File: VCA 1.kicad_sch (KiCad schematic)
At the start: 87 parts, among them J1 Eurorack 2x8hs, J10 CV2, J11 IN2, J12 IN 1x8h, J13 OUT1, J14 OUT2, J15 IN 1x8s, J2 OUT 1x3s, J3 CV 1x9s, J5 CV 1x9h, J6 OUT 1x3h, J8 CV1, J9 IN1, Q1 2N3904, Q2 2N3904, U1 TL074, U2 AS2164

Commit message: Updated schematic and image
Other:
- moved on the sheet: C12, J10, R13, R14, R15, R16, R24, RV10, RV2, RV4, RV9, U1B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

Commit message: Noted linearization components
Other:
- note added: "Linearization 1 A"
- note added: "Linearization 1 B"
- note added: "Linearization 2 A"
- note added: "Linearization 2 B"
- note removed: "VCA 2 Input"
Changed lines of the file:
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@@
 	)
 	(rectangle
-		(start 17.145 117.475)
-		(end 251.46 236.22)
+		(start 15.24 205.105)
+		(end 80.01 234.315)
 		(stroke
 			(width 0)
@@
 	)
 	(rectangle
-		(start 17.145 13.97)
-		(end 251.46 117.475)
+		(start 17.145 43.18)
+		(end 81.915 72.39)
 		(stroke
 			(width 0)
@@
 	(text "Curve 2"
 		(exclude_from_sim no)
-		(at 140.462 142.494 0)
+		(at 135.382 156.972 0)
 		(effects
 			(font
@@
 		)
 	)
+	(text "Linearization 2 A"
+		(exclude_from_sim no)
+		(at 24.638 232.41 0)
+		(effects
+			(font
+				(size 1.27 1.27)
+			)
+		)
+	)
 	(text "Offset 2"
 		(exclude_from_sim no)
@@
 	(text "Curve 1"
 		(exclude_from_sim no)
-		(at 141.224 104.394 0)
+		(at 134.366 118.618 0)
+		(effects
+			(font
+				(size 1.27 1.27)
+			)
+		)
+	)
+	(text "Linearization 1 B"
+		(exclude_from_sim no)
+		(at 138.938 104.648 0)
 		(effects
 			(font
@@
 	(text "VCA 2 Output"
 		(exclude_from_sim no)
-		(at 299.466 144.018 0)
+		(at 260.096 98.298 0)
 		(effects
 			(font
@@
 	(text "VCA 1 Output"
 		(exclude_from_sim no)
-		(at 298.958 32.512 0)
+		(at 260.096 91.694 0)
 		(effects
 			(font
@@
 		)
 	)
+	(text "Linearization 2 B"
+		(exclude_from_sim no)
+		(at 139.7 143.002 0)
+		(effects
+			(font
+				(size 1.27 1.27)
+			)
+		)
+	)
 	(text "Hagiwo"
 		(exclude_from_sim yes)
@@
 		)
 	)
-	(text "VCA 1 Input"
+	(text "Linearization 1 A"
 		(exclude_from_sim no)
-		(at 25.4 17.78 0)
+		(at 26.924 71.12 0)
 		(effects
 			(font
@@
 		)
 	)
-	(text "Dual VCA I (main and control boards)"
+	(text "VCA 1 Input"
 		(exclude_from_sim no)
-		(at 347.726 276.606 0)
+		(at 136.398 53.086 0)
 		(effects
 			(font
-				(size 2.54 2.54)
+				(size 1.27 1.27)
 			)
 		)
 	)
-	(text "Offset 1"
+	(text "Dual VCA I (main and control boards)"
 		(exclude_from_sim no)
-		(at 23.622 102.87 0)
+		(at 347.726 276.606 0)
 		(effects
 			(font
-				(size 1.27 1.27)
+				(size 2.54 2.54)
 			)
 		)
 	)
-	(text "VCA 2 Input"
+	(text "Offset 1"
 		(exclude_from_sim no)
-		(at 25.146 233.426 0)
+		(at 23.622 102.87 0)
 		(effects
 			(font
@@
 	)
 	(junction
+		(at 73.66 195.58)
+		(diameter 0)
+		(color 0 0 0 0)
+	)
+	(junction
 		(at 140.97 243.84)
 		(diameter 0)
@@
 	)
 	(junction
-		(at 78.74 195.58)
-		(diameter 0)
-		(color 0 0 0 0)
-	)
-	(junction
 		(at 201.93 274.32)
 		(diameter 0)
@@
 		)
 	)
+	(polyline
+		(pts
+			(xy 130.81 140.335) (xy 130.81 160.02)
+		)
+		(stroke
+			(width 0)
+			(type default)
+		)
+	)
 	(wire
 		(pts
@@
 		)
 	)
+	(polyline
+		(pts
+			(xy 203.835 119.38) (xy 156.845 119.38)
+		)
+		(stroke
+			(width 0)
+			(type default)
+		)
+	)
 	(wire
 		(pts
@@
 	(wire
 		(pts
-			(xy 78.74 195.58) (xy 146.05 195.58)
-		)
-		(stroke
-			(width 0)
-			(type default)
-		)
-	)
-	(wire
-		(pts
 			(xy 24.13 187.96) (xy 24.13 191.77)
 		)
@@
 		)
 	)
+	(polyline
+		(pts
+			(xy 152.4 120.65) (xy 152.4 116.84)
+		)
+		(stroke
+			(width 0)
+			(type default)
+		)
+	)
 	(wire
 		(pts
@@
 		)
 	)
+	(polyline
+		(pts
+			(xy 129.54 102.87) (xy 151.13 102.87)
+		)
+		(stroke
+			(width 0)
+			(type default)
+		)
+	)
 	(wire
 		(pts
@@
 		)
 	)
+	(polyline
+		(pts
+			(xy 129.54 120.65) (xy 152.4 120.65)
+		)
+		(stroke
+			(width 0)
+			(type default)
+		)
+	)
 	(wire
 		(pts
@@
 		)
 	)
+	(polyline
+		(pts
+			(xy 250.19 98.425) (xy 223.52 98.425)
+		)
+		(stroke
+			(width 0)
+			(type default)
+		)
+	)
 	(wire
 		(pts
@@
 	(wire
 		(pts
-			(xy 78.74 218.44) (xy 69.85 218.44)
+			(xy 73.66 218.44) (xy 69.85 218.44)
 		)
 		(stroke
@@
 		)
 	)
+	(polyline
+		(pts
+			(xy 152.4 116.84) (xy 250.19 116.84)
+		)
+		(stroke
+			(width 0)
+			(type default)
+		)
+	)
 	(wire
 		(pts
@@
 	(wire
 		(pts
-			(xy 78.74 195.58) (xy 78.74 218.44)
+			(xy 73.66 195.58) (xy 73.66 218.44)
 		)
 		(stroke
@@
 		)
 	)
+	(polyline
+		(pts
+			(xy 156.845 119.38) (xy 156.845 140.335)
+		)
+		(stroke
+			(width 0)
+			(type default)
+		)
+	)
 	(wire
 		(pts
@@
 		)
 	)
+	(polyline
+		(pts
+			(xy 223.52 109.22) (xy 151.13 109.22)
+		)
+		(stroke
+			(width 0)
+			(type default)
+		)
+	)
 	(wire
 		(pts
@@
 	(wire
 		(pts
+			(xy 73.66 195.58) (xy 146.05 195.58)
+		)
+		(stroke
+			(width 0)
+			(type default)
+		)
+	)
+	(wire
+		(pts
 			(xy 140.97 243.84) (xy 127 243.84)
 		)
@@
 		)
 	)
+	(polyline
+		(pts
+			(xy 130.81 160.02) (xy 203.835 160.02)
+		)
+		(stroke
+			(width 0)
+			(type default)
+		)
+	)
 	(wire
 		(pts
@@
 		)
 	)
+	(polyline
+		(pts
+			(xy 151.13 109.22) (xy 151.13 102.87)
+		)
+		(stroke
+			(width 0)
+			(type default)
+		)
+	)
 	(wire
 		(pts
@@
 	(wire
 		(pts
-			(xy 41.91 195.58) (xy 78.74 195.58)
+			(xy 41.91 195.58) (xy 73.66 195.58)
+		)
+		(stroke
+			(width 0)
+			(type default)
+		)
+	)
+	(polyline
+		(pts
+			(xy 250.19 116.84) (xy 250.19 98.425)
 		)
 		(stroke
@@
 		)
 	)
+	(polyline
+		(pts
+			(xy 203.835 160.02) (xy 203.835 119.38)
+		)
+		(stroke
+			(width 0)
+			(type default)
+		)
+	)
 	(wire
 		(pts
@@
 		)
 	)
+	(polyline
+		(pts
+			(xy 156.845 140.335) (xy 130.81 140.335)
+		)
+		(stroke
+			(width 0)
+			(type default)
+		)
+	)
 	(wire
 		(pts
@@
 		)
 	)
+	(polyline
+		(pts
+			(xy 223.52 98.425) (xy 223.52 109.22)
+		)
+		(stroke
+			(width 0)
+			(type default)
+		)
+	)
 	(wire
 		(pts
@@
 		)
 	)
+	(polyline
+		(pts
+			(xy 129.54 102.87) (xy 129.54 120.65)
+		)
+		(stroke
+			(width 0)
+			(type default)
+		)
+	)
 	(global_label "+12v"
 		(shape input)
@@
 		)
 	)
+	(group ""
+		(members "18a44e6c-de5b-467a-8f2e-db9e40b2f192" "26d99882-d493-48b8-8b53-ef1b25249a56"
+			"335e110c-c7a5-42e0-965f-61530e30d26d" "35f6677c-5b62-4938-b17b-062d7b1850b7"
+			"7b091e6f-4273-460f-bf15-8d6bc277b69b" "a904838e-bbb1-44ab-9fbb-02d583ba5790"
+			"b56eea77-ddf2-493a-affa-bebb6470614a" "d29784d0-988b-4366-947c-30e8e71c4bf2"
+			"f483f174-9161-47e0-90b6-0b6b0535353c" "ff328fe6-7960-4840-bb69-712337915f44"
+		)
+	)
+	(group ""
+		(members "01b665f1-7e63-4283-a37a-9746674eea88" "06bd41dc-a293-40ec-972a-06a894a96dc2"
+			"9f5f978c-7975-466a-84ba-87b8600012bb" "b4068527-1d47-46ce-bbba-b00ad5667bf6"
+			"ea6af55a-41a7-4d35-8ed7-e8c048290715" "f143c6ff-58e2-4165-997b-5711abf60db6"
+		)
+	)

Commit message: New simulation, updated design after breadboard test.
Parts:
- added R19, R20: 390R, Resistor_THT:R_Axial_DIN0204_L3.6mm_D1.6mm_P2.54mm_Vertical, symbol Device:R
- R24, R8: value 2K2 -> 3K3
- RV5, RV6: value 10K B -> 1K B
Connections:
- net at U2.6 (CV): now also R19.1; no longer J15.3 (Pin_3)
- net at J15.7 (Pin_7): now also R20.2; no longer U2.14 (CV)
- new net: J15.3 (Pin_3), R19.2
- new net: R20.1, U2.14 (CV)
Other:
- note added: "Curve selection 1"
- note added: "Curve selection 2"
- note added: "Input stage 1"
- note added: "Input stage 2"
- note added: "Linearization 1"
- note added: "Linearization 2"
- note added: "Output 1"
- note added: "Output 2"
- note removed: "Linearization 1 A"
- note removed: "Linearization 1 B"
- note removed: "Linearization 2 A"
- note removed: "Linearization 2 B"
- note removed: "VCA 1 Output"
- note removed: "VCA 2 Output"
- moved on the sheet: J10, RV2, RV4

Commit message: Updated curve values to match breadboard
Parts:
- added C15, C16: 10uF t, Capacitor_THT:CP_Radial_Tantal_D4.5mm_P2.50mm, symbol Device:C_Polarized
- R24, R8: value 3K3 -> 2K2
- RV5, RV6: value 1K B -> 10K B
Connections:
- net at R10.1, U2.2 (IN): now also C15.2; no longer R9.2
- net at R18.1, U2.10 (IN): now also C16.2; no longer R17.2
- new net: C16.1, R17.2
- new net: C15.1, R9.2
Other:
- moved on the sheet: C10, C13, R10, R18, R9

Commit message: Removed uneeded resistor
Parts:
- removed R19, R20: 390R, Resistor_THT:R_Axial_DIN0204_L3.6mm_D1.6mm_P2.54mm_Vertical, symbol Device:R
- R18: footprint Resistor_THT:R_Axial_DIN0204_L3.6mm_D1.6mm_P7.62mm_Horizontal -> Resistor_THT:R_Axial_DIN0204_L3.6mm_D1.6mm_P2.54mm_Vertical
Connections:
- net at U2.6 (CV): now also J15.3 (Pin_3)
- net at J15.7 (Pin_7): now also U2.14 (CV)
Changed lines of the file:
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@@
 	(wire
 		(pts
-			(xy 205.74 144.78) (xy 205.74 227.33)
+			(xy 205.74 123.19) (xy 205.74 227.33)
 		)
 		(stroke
@@
 	(wire
 		(pts
-			(xy 209.55 113.03) (xy 210.82 113.03)
-		)
-		(stroke
-			(width 0)
-			(type default)
-		)
-	)
-	(wire
-		(pts
 			(xy 321.31 52.07) (xy 314.96 52.07)
 		)
@@
 	(wire
 		(pts
-			(xy 199.39 113.03) (xy 201.93 113.03)
+			(xy 199.39 113.03) (xy 210.82 113.03)
 		)
 		(stroke
@@
 		)
 	)
-	(wire
-		(pts
-			(xy 205.74 123.19) (xy 205.74 137.16)
-		)
-		(stroke
-			(width 0)
-			(type default)
-		)
-	)
 	(polyline
 		(pts
@@
 			)
 		)
-		(property "Footprint" "Resistor_THT:R_Axial_DIN0204_L3.6mm_D1.6mm_P7.62mm_Horizontal"
+		(property "Footprint" "Resistor_THT:R_Axial_DIN0204_L3.6mm_D1.6mm_P2.54mm_Vertical"
 			(at 247.142 133.35 90)
 			(hide yes)
@@
 	)
 	(symbol
-		(lib_id "Device:R")
-		(at 205.74 113.03 270)
-		(unit 1)
-		(body_style 1)
-		(exclude_from_sim no)
-		(in_bom yes)
-		(on_board yes)
-		(in_pos_files yes)
-		(dnp no)
-		(fields_autoplaced yes)
-		(property "Reference" "R19"
-			(at 205.74 106.68 90)
-			(show_name no)
-			(do_not_autoplace no)
-			(effects
-				(font
-					(size 1.27 1.27)
-				)
-			)
-		)
-		(property "Value" "390R"
-			(at 205.74 109.22 90)
-			(show_name no)
-			(do_not_autoplace no)
-			(effects
-				(font
-					(size 1.27 1.27)
-				)
-			)
-		)
-		(property "Footprint" "Resistor_THT:R_Axial_DIN0204_L3.6mm_D1.6mm_P2.54mm_Vertical"
-			(at 205.74 111.252 90)
-			(hide yes)
-			(show_name no)
-			(do_not_autoplace no)
-			(effects
-				(font
-					(size 1.27 1.27)
-				)
-			)
-		)
-		(property "Datasheet" ""
-			(at 205.74 113.03 0)
-			(hide yes)
-			(show_name no)
-			(do_not_autoplace no)
-			(effects
-				(font
-					(size 1.27 1.27)
-				)
-			)
-		)
-		(property "Description" "Resistor"
-			(at 205.74 113.03 0)
-			(hide yes)
-			(show_name no)
-			(do_not_autoplace no)
-			(effects
-				(font
-					(size 1.27 1.27)
-				)
-			)
-		)
-		(pin "2"
-		)
-		(pin "1"
-		)
-		(instances
-			(project "VCA 1"
-				(path "/eb1652b6-57da-4a0e-88a4-449907a19840"
-					(reference "R19")
-					(unit 1)
-				)
-			)
-		)
-	)
-	(symbol
 		(lib_id "Connector_Audio:AudioJack2_SwitchT")
 		(at 25.4 140.97 0)
@@
 					(unit 1)
 				)
-			)
-		)
-	)
-	(symbol
-		(lib_id "Device:R")
-		(at 205.74 140.97 180)
-		(unit 1)
-		(body_style 1)
-		(exclude_from_sim no)
-		(in_bom yes)
-		(on_board yes)
-		(in_pos_files yes)
-		(dnp no)
-		(fields_autoplaced yes)
-		(property "Reference" "R20"
-			(at 208.28 139.6999 0)
-			(show_name no)
-			(do_not_autoplace no)
-			(effects
-				(font
-					(size 1.27 1.27)
-				)
-				(justify right)
-			)
-		)
-		(property "Value" "390R"
-			(at 208.28 142.2399 0)
-			(show_name no)
-			(do_not_autoplace no)
-			(effects
-				(font
-					(size 1.27 1.27)
-				)
-				(justify right)
-			)
-		)
-		(property "Footprint" "Resistor_THT:R_Axial_DIN0204_L3.6mm_D1.6mm_P2.54mm_Vertical"
-			(at 207.518 140.97 90)
-			(hide yes)
-			(show_name no)
-			(do_not_autoplace no)
-			(effects
-				(font
-					(size 1.27 1.27)
-				)
-			)
-		)
-		(property "Datasheet" ""
-			(at 205.74 140.97 0)
-			(hide yes)
-			(show_name no)
-			(do_not_autoplace no)
-			(effects
-				(font
-					(size 1.27 1.27)
-				)
-			)
-		)
-		(property "Description" "Resistor"
-			(at 205.74 140.97 0)
-			(hide yes)
-			(show_name no)
-			(do_not_autoplace no)
-			(effects
-				(font
-					(size 1.27 1.27)
-				)
-			)
-		)
-		(pin "2"
-		)
-		(pin "1"
-		)
-		(instances
-			(project "VCA 1"
-				(path "/eb1652b6-57da-4a0e-88a4-449907a19840"
-					(reference "R20")
-					(unit 1)
-				)

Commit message: Reworked R values for 0-8V CV
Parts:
- R15, R6: value 33K -> 10K
- R24, R8: value 2K2 -> 15K
- RV8: value 10K -> 20K
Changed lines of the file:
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@@
 	(text "Offset 2"
 		(exclude_from_sim no)
-		(at 24.13 140.97 0)
+		(at 20.828 122.174 0)
 		(effects
 			(font
@@
 		(fields_autoplaced yes)
 		(property "Reference" "R6"
-			(at 40.64 36.83 90)
+			(at 40.64 26.67 90)
 			(show_name no)
 			(do_not_autoplace no)
@@
 			)
 		)
-		(property "Value" "33K"
-			(at 40.64 39.37 90)
+		(property "Value" "10K"
+			(at 40.64 29.21 90)
 			(show_name no)
 			(do_not_autoplace no)
@@
 		(fields_autoplaced yes)
 		(property "Reference" "R15"
-			(at 38.1 199.39 90)
+			(at 38.1 189.23 90)
 			(show_name no)
 			(do_not_autoplace no)
@@
 			)
 		)
-		(property "Value" "33K"
-			(at 38.1 201.93 90)
+		(property "Value" "10K"
+			(at 38.1 191.77 90)
 			(show_name no)
 			(do_not_autoplace no)
@@
 			)
 		)
-		(property "Value" "10K"
+		(property "Value" "20K"
 			(at 24.13 57.1499 0)
 			(show_name no)
@@
 			)
 		)
-		(property "Value" "2K2"
+		(property "Value" "15K"
 			(at 203.2 142.2399 0)
 			(show_name no)
@@
 			)
 		)
-		(property "Value" "2K2"
+		(property "Value" "15K"
 			(at 240.03 99.06 90)
 			(show_name no)

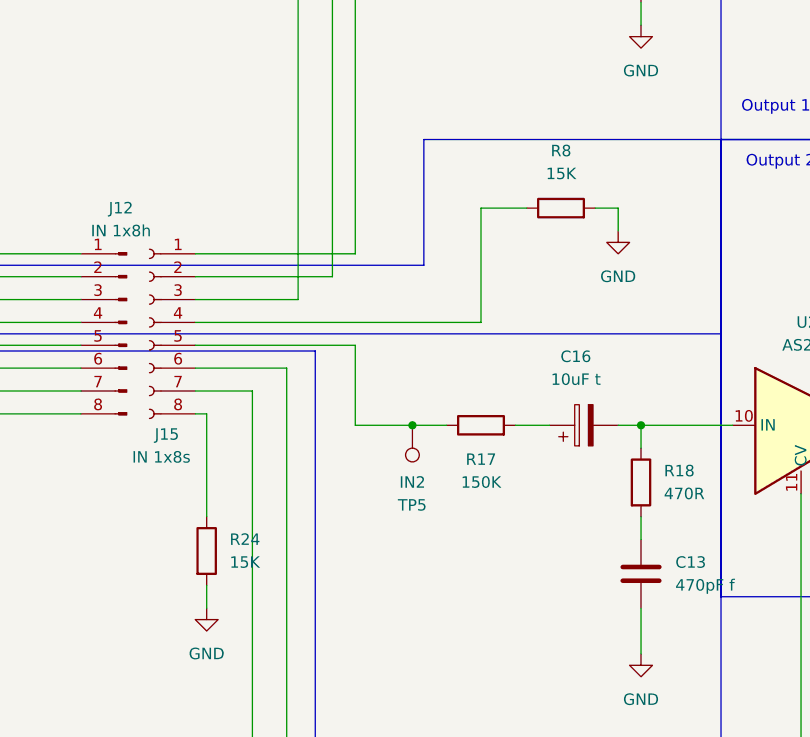
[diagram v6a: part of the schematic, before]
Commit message: Updated Curve to GND R
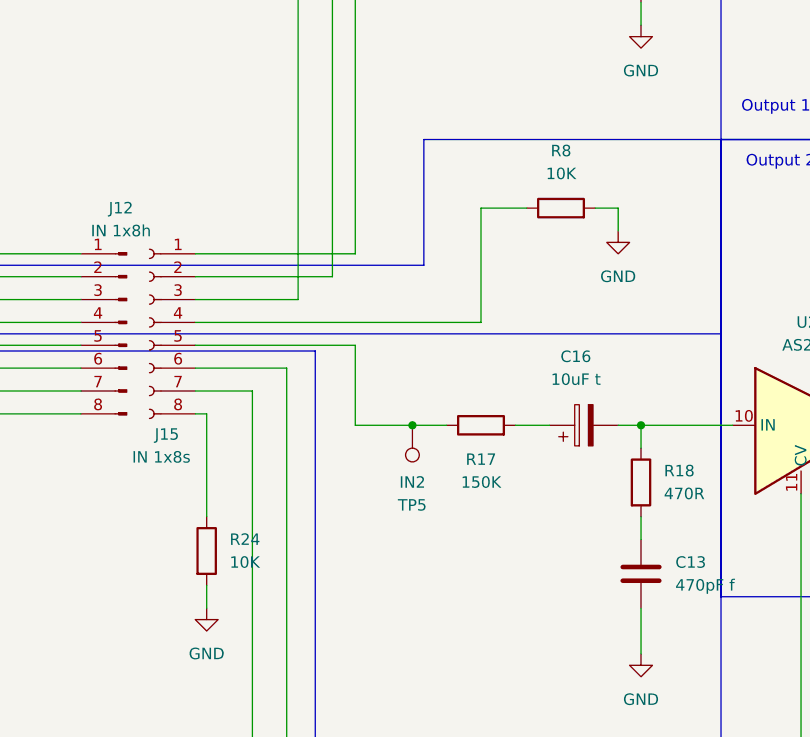
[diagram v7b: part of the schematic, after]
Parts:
- R24, R8: value 15K -> 10K
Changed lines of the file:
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@@
 			)
 		)
-		(property "Value" "15K"
+		(property "Value" "10K"
 			(at 203.2 142.2399 0)
 			(show_name no)
@@
 			)
 		)
-		(property "Value" "15K"
+		(property "Value" "10K"
 			(at 240.03 99.06 90)
 			(show_name no)

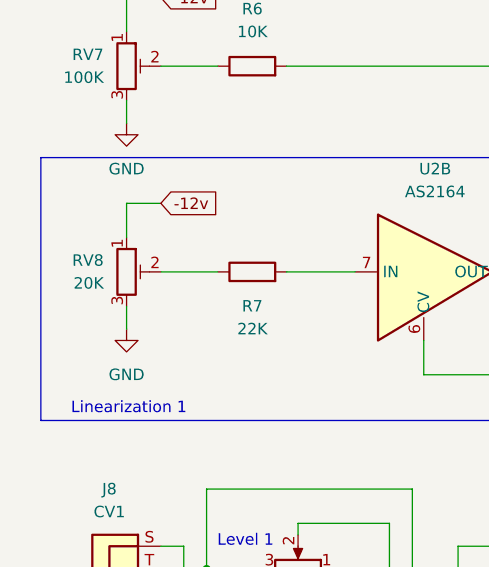
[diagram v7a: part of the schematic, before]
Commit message: Returned Lin input RV to 10K
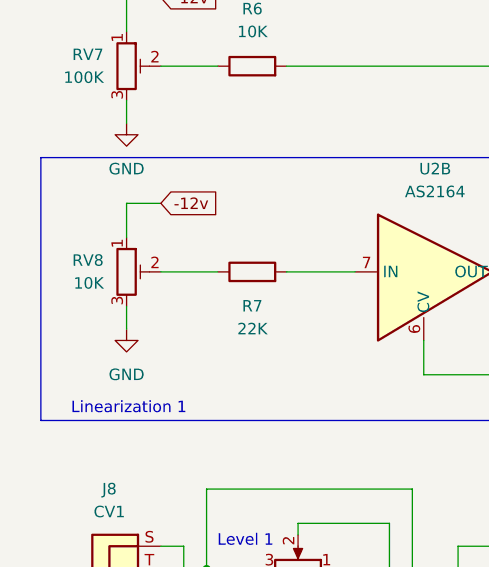
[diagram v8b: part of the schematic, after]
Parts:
- RV8: value 20K -> 10K
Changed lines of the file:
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@@
 			)
 		)
-		(property "Value" "20K"
+		(property "Value" "10K"
 			(at 24.13 57.1499 0)
 			(show_name no)
